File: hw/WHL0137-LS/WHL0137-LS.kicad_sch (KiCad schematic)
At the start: 0 parts

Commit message: Initial schematic
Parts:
- added D73: LED_Small, LED_SMD:LED_0805_2012Metric, symbol Device:LED_Small
- added J1: Conn_01x05, Connector_JST:JST_EH_S5B-EH_1x05_P2.50mm_Horizontal, symbol Connector_Generic:Conn_01x05
- added R5: 510, Resistor_SMD:R_0805_2012Metric, symbol Device:R
- added TP1, TP2: TestPoint, TestPoint:TestPoint_Pad_D2.5mm, symbol Connector:TestPoint
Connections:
- new net: D73.2 (A), R5.2
- new net +5V: J1.1 (Pin_1), R5.1, TP1.1
- new net GND: D73.1 (K), J1.5 (Pin_5), TP2.1
- new net inner_LED_ring/SCL: J1.3 (Pin_3)
- new net inner_LED_ring/SDA: J1.2 (Pin_2)
- new net inner_LED_ring/SDB: J1.4 (Pin_4)
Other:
- added sheet inner_LED_ring (LED_ring.kicad_sch)
- added sheet outer_LED_ring (LED_ring.kicad_sch)
- title: (none) -> WHL0137-LS

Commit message: Some layout
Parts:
- added R2: 100k, Resistor_SMD:R_0805_2012Metric, symbol Device:R
- renumbered R5 to R1
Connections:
- net GND: now also R2.2
- net inner_LED_ring/SDB: now also R2.1
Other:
- moved on the sheet: D73, J1, R1, TP1, TP2

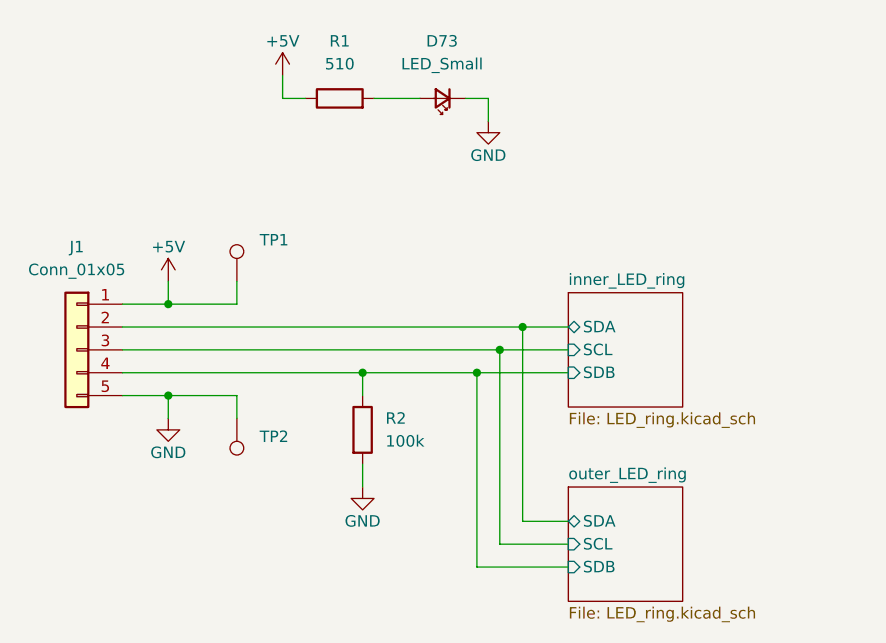
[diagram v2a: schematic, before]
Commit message: Routed LED traces and fixed designators
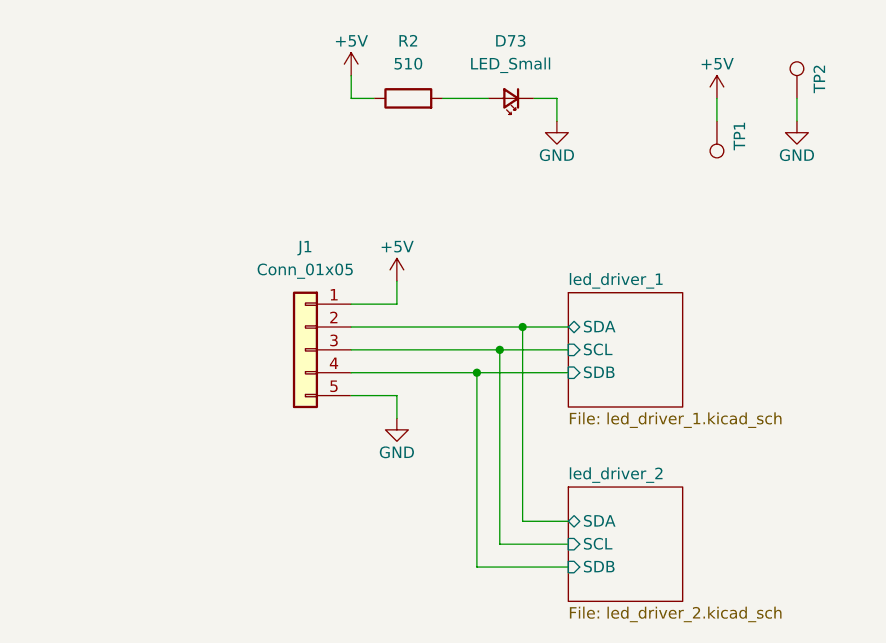
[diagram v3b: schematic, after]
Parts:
- removed R2: 100k, Resistor_SMD:R_0805_2012Metric, symbol Device:R
- renumbered R1 to R2
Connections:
- net inner_LED_ring/SCL renamed led_driver_1/SCL
- net inner_LED_ring/SDA renamed led_driver_1/SDA
- net inner_LED_ring/SDB renamed led_driver_1/SDB
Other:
- removed sheet inner_LED_ring
- removed sheet outer_LED_ring
- added sheet led_driver_1 (led_driver_1.kicad_sch)
- added sheet led_driver_2 (led_driver_2.kicad_sch)
- moved on the sheet: D73, J1, R2, TP1, TP2

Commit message: misc changes
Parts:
- removed TP1, TP2: TestPoint, TestPoint:TestPoint_Pad_D2.5mm, symbol Connector:TestPoint
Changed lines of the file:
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@@
-    (stroke (width 0) (type default) (color 0 0 0 0))
-  )
-  (wire (pts (xy 181.61 62.23) (xy 181.61 64.77))
     (stroke (width 0) (type default) (color 0 0 0 0))
   )
@@
     (stroke (width 0) (type default) (color 0 0 0 0))
   )
-  (wire (pts (xy 172.72 62.23) (xy 172.72 64.77))
-    (stroke (width 0) (type default) (color 0 0 0 0))
-  )
   (wire (pts (xy 137.16 97.79) (xy 137.16 95.25))
     (stroke (width 0) (type default) (color 0 0 0 0))
-  )
-  (symbol (lib_id "power:+5V") (at 172.72 62.23 0) (unit 1)
-    (in_bom yes) (on_board yes)
-    (property "Reference" "#PWR029" (id 0) (at 172.72 66.04 0)
-      (effects (font (size 1.27 1.27)) hide)
-    )
-    (property "Value" "+5V" (id 1) (at 172.72 58.42 0))
-    (property "Footprint" "" (id 2) (at 172.72 62.23 0)
-      (effects (font (size 1.27 1.27)) hide)
-    )
-    (property "Datasheet" "" (id 3) (at 172.72 62.23 0)
-      (effects (font (size 1.27 1.27)) hide)
-    )
-    (pin "1")
   )
   (symbol (lib_id "power:+5V") (at 137.16 82.55 0) (unit 1)
@@
     )
     (property "Datasheet" "" (id 3) (at 137.16 82.55 0)
-      (effects (font (size 1.27 1.27)) hide)
-    )
-    (pin "1")
-  )
-  (symbol (lib_id "power:GND") (at 181.61 64.77 0) (unit 1)
-    (in_bom yes) (on_board yes)
-    (property "Reference" "#PWR030" (id 0) (at 181.61 71.12 0)
-      (effects (font (size 1.27 1.27)) hide)
-    )
-    (property "Value" "GND" (id 1) (at 181.61 68.58 0))
-    (property "Footprint" "" (id 2) (at 181.61 64.77 0)
-      (effects (font (size 1.27 1.27)) hide)
-    )
-    (property "Datasheet" "" (id 3) (at 181.61 64.77 0)
       (effects (font (size 1.27 1.27)) hide)
     )
@@
     (pin "5")
   )
-  (symbol (lib_id "Connector:TestPoint") (at 181.61 62.23 0) (mirror y) (unit 1)
-    (in_bom yes) (on_board yes)
-    (property "Reference" "TP2" (id 0) (at 184.15 58.42 90)
-      (effects (font (size 1.27 1.27)) (justify right))
-    )
-    (property "Value" "TestPoint" (id 1) (at 184.15 57.6581 0)
-      (effects (font (size 1.27 1.27)) (justify right) hide)
-    )
-    (property "Footprint" "TestPoint:TestPoint_Pad_D2.5mm" (id 2) (at 176.53 62.23 0)
-      (effects (font (size 1.27 1.27)) hide)
-    )
-    (property "Datasheet" "~" (id 3) (at 176.53 62.23 0)
-      (effects (font (size 1.27 1.27)) hide)
-    )
-    (pin "1")
-  )
   (symbol (lib_id "Device:R") (at 138.43 62.23 90) (unit 1)
     (in_bom yes) (on_board yes) (fields_autoplaced)
@@
     (pin "2")
   )
-  (symbol (lib_id "Connector:TestPoint") (at 172.72 64.77 180) (unit 1)
-    (in_bom yes) (on_board yes)
-    (property "Reference" "TP1" (id 0) (at 175.26 64.77 90)
-      (effects (font (size 1.27 1.27)) (justify left))
-    )
-    (property "Value" "TestPoint" (id 1) (at 170.18 66.8021 0)
-      (effects (font (size 1.27 1.27)) (justify left) hide)
-    )
-    (property "Footprint" "TestPoint:TestPoint_Pad_D2.5mm" (id 2) (at 167.64 64.77 0)
-      (effects (font (size 1.27 1.27)) hide)
-    )
-    (property "Datasheet" "~" (id 3) (at 167.64 64.77 0)
-      (effects (font (size 1.27 1.27)) hide)
-    )
-    (pin "1")
-  )
   (symbol (lib_id "power:GND") (at 154.94 64.77 0) (unit 1)
     (in_bom yes) (on_board yes)
@@
       (reference "#PWR028") (unit 1) (value "GND") (footprint "")
     )
-    (path "/023e97e3-0ec0-4c76-8c99-de28337e6bda"
-      (reference "#PWR029") (unit 1) (value "+5V") (footprint "")
-    )
-    (path "/27988ba4-0afa-409e-b989-7d88526b4654"
-      (reference "#PWR030") (unit 1) (value "GND") (footprint "")
-    )
     (path "/8b98f270-a8d0-4731-a1df-c03e894b43cf/50bc36fd-7783-4308-a5c5-e51dc221047e"
       (reference "C1") (unit 1) (value "0.1u") (footprint "Capacitor_SMD:C_0805_2012Metric")
@@
       (reference "R3") (unit 1) (value "3.3k") (footprint "Resistor_SMD:R_0805_2012Metric")
     )
-    (path "/e4c5e7ff-f9d5-42b2-8a8b-4f0217e476d4"
-      (reference "TP1") (unit 1) (value "TestPoint") (footprint "TestPoint:TestPoint_Pad_D2.5mm")
-    )
-    (path "/b6256f16-ec42-412b-84e8-067184d216f3"
-      (reference "TP2") (unit 1) (value "TestPoint") (footprint "TestPoint:TestPoint_Pad_D2.5mm")
-    )
     (path "/8b98f270-a8d0-4731-a1df-c03e894b43cf/9c1547f5-19b6-4728-885d-9f730c56d185"
